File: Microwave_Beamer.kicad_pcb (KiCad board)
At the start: 6 copper layers, 200 x 170 mm, 471 parts, among them IC1 MAX2870ETJ+, J1 SMA-J-P-H-ST-EM1, J2 SMA-J-P-H-ST-EM1, J3 4pos_TH, J4 4pos_TH, J5 4pos_TH, J6 4pos_TH, J7 4pos_TH, J8 PJ-002A, SW1 PTS526SM15SMTR2 LFS, SW2 PTS526SM15SMTR2 LFS, U1 SKY13575-639LF, U10 SKY13575-639LF, U11 SKY13575-639LF, U12 SKY13575-639LF, U13 SE5023L-R, U14 SE5023L-R, U15 SE5023L-R, U16 SE5023L-R, U17 SE5023L-R, U18 SE5023L-R, U19 SE5023L-R, U2 SKY13575-639LF, U20 SE5023L-R, U21 SE5023L-R, U22 SE5023L-R, U23 SE5023L-R, U24 SE5023L-R, U25 SE5023L-R, U26 SE5023L-R, U27 SE5023L-R, U28 SE5023L-R, U29 SE5023L-R, U3 SKY13575-639LF, U30 SE5023L-R, U31 SE5023L-R, U32 SE5023L-R, U33 SE5023L-R, U34 SE5023L-R, U35 SE5023L-R, U36 SE5023L-R, U37 SE5023L-R, U38 SE5023L-R, U39 SE5023L-R, U4 SKY13575-639LF, U40 SE5023L-R, U41 SE5023L-R, U42 SE5023L-R, U43 SE5023L-R, U44 SE5023L-R, U45 SE5023L-R, U46 SE5023L-R, U47 SE5023L-R, U48 SE5023L-R, U49 SE5023L-R, U5 SKY13575-639LF, U50 LDL1117S33R, U51 SN74LVC1G14DCKR, U52 MIC5219-2.85YM5-TR, U53 SN74LVC1G14DCKR, U54 74HC138D, U55 TPS548D26RXXR, U56 PI_PICO, U57 SN74LVC1G14DCKR, U58 LMH2120UM/NOPB, U6 SKY13575-639LF, U7 SKY13575-639LF, U8 SKY13575-639LF, U9 SKY13575-639LF, Y1 ECS-3225MVQ-1000-CN-TR

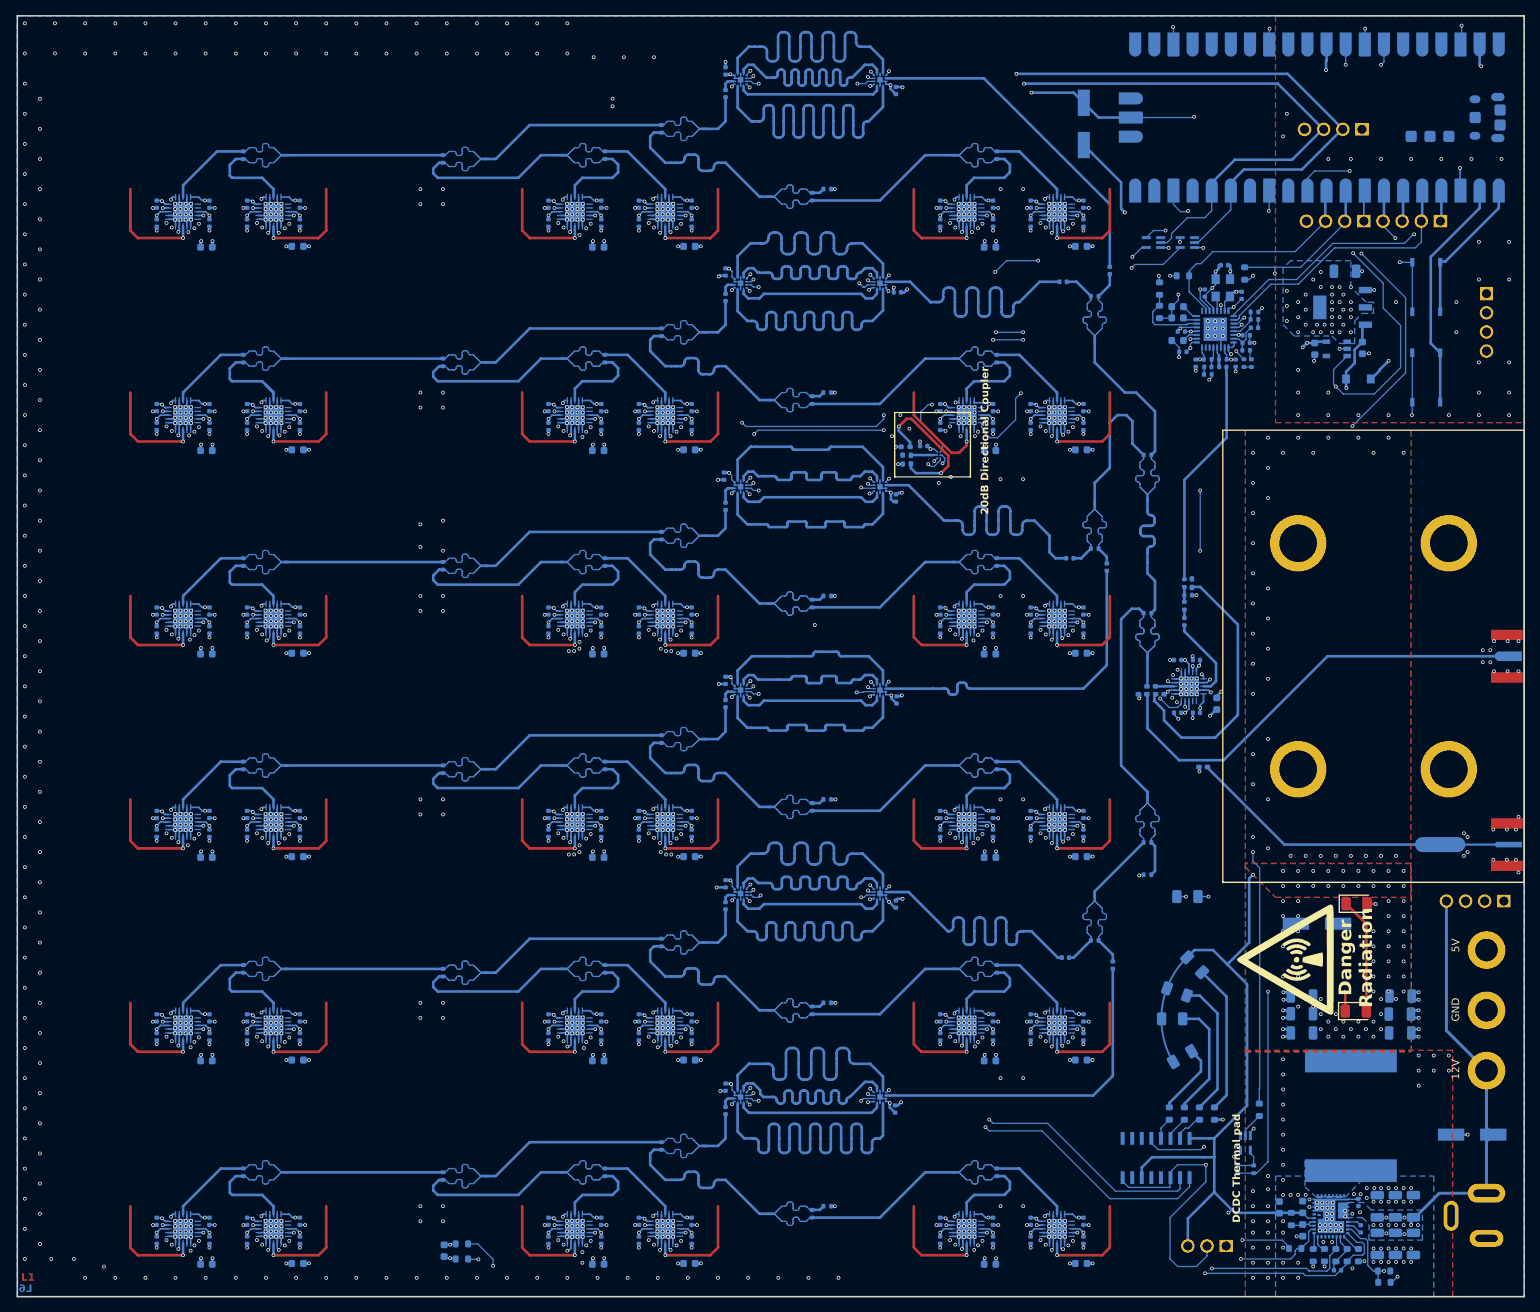
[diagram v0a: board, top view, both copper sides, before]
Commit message: created version with standard stackup
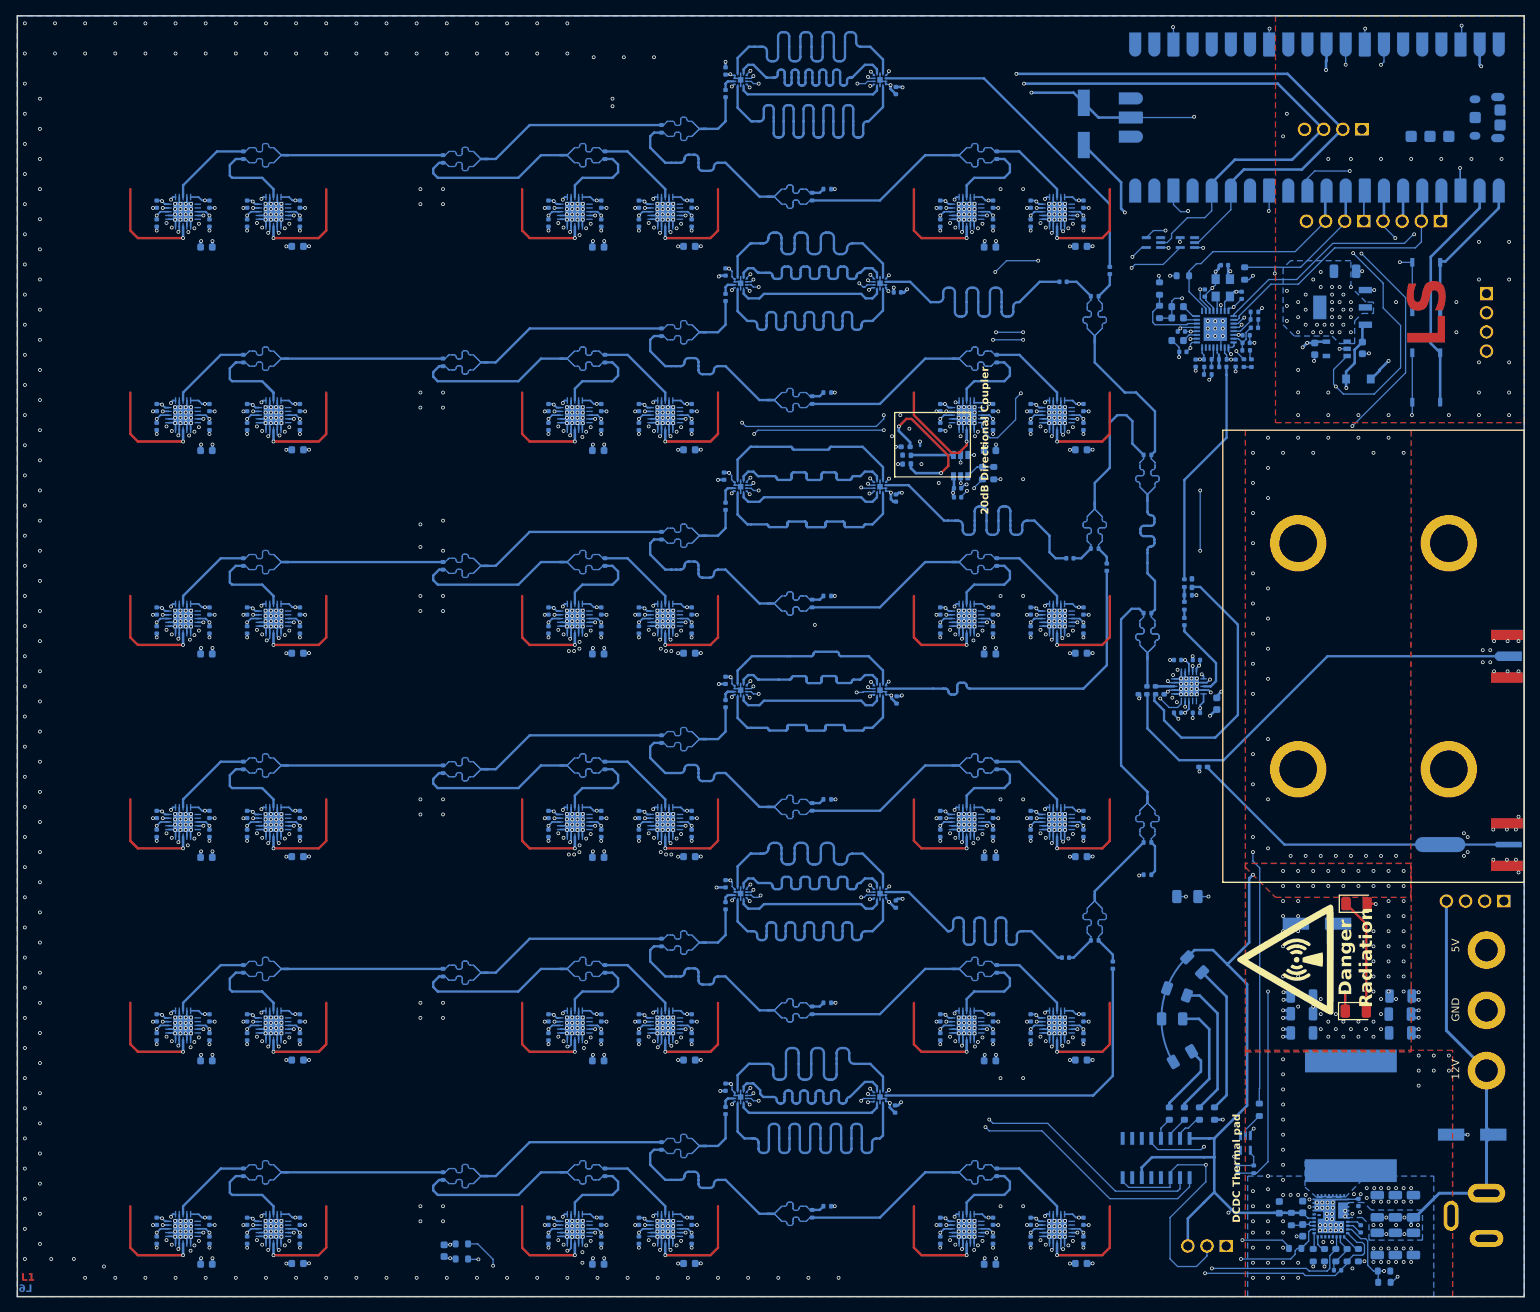
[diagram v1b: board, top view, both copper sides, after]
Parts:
- removed the U58 at (132.3, 63.3)
- added C282: 1nF, Capacitor_SMD:C_0402_1005Metric, B.Cu at (134.8, 67.7)
- added R79: 1k, Resistor_SMD:R_0603_1608Metric, B.Cu at (139.6, 65.7)
- added R80: 1k, Resistor_SMD:R_0603_1608Metric, B.Cu at (138.1, 65.7)
- added U59: LTC5531ES6-TRMPBF, RF_components:SOT-6_S_LIT-M, B.Cu at (135.2, 64.7)
- moved C331 8.15 mm to (134.8, 68.9), turned to 0 degrees
- renumbered IC1 to U58, PS1 to U60, Y1 to X1
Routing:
- net +3.3V: track 405.1 -> 412.2 mm, vias 102 -> 103
- net coupled power: track 96.6 -> 101.0 mm
- net Net-(U59-VOS): track 0.00 -> 3.96 mm
- net Net-(U59-RFIN): track 3.51 -> 5.67 mm
- net GND: track 684.6 -> 686.6 mm, vias 1454 -> 1455
- net +12V: vias 15 -> 13
- added copper zone on In3.Cu, net GND
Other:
- board text added: "LS"
